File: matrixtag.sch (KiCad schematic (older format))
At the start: 23 parts

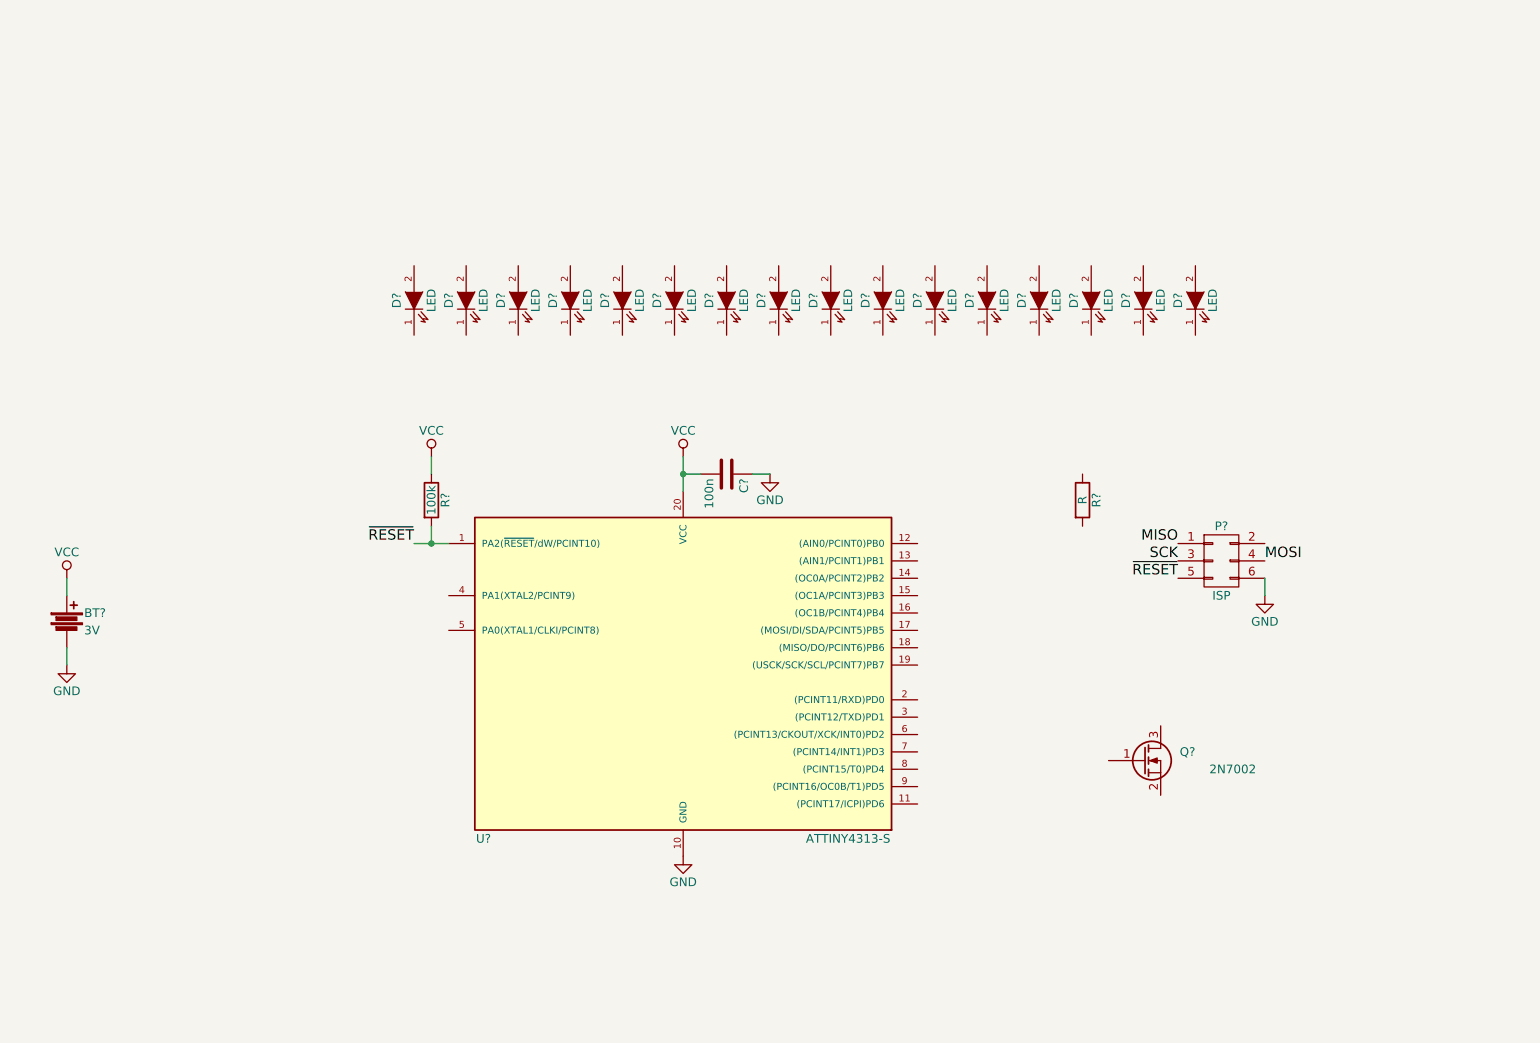
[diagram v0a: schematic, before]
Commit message: Added schematics and unrouted PCB of matrix display nametag
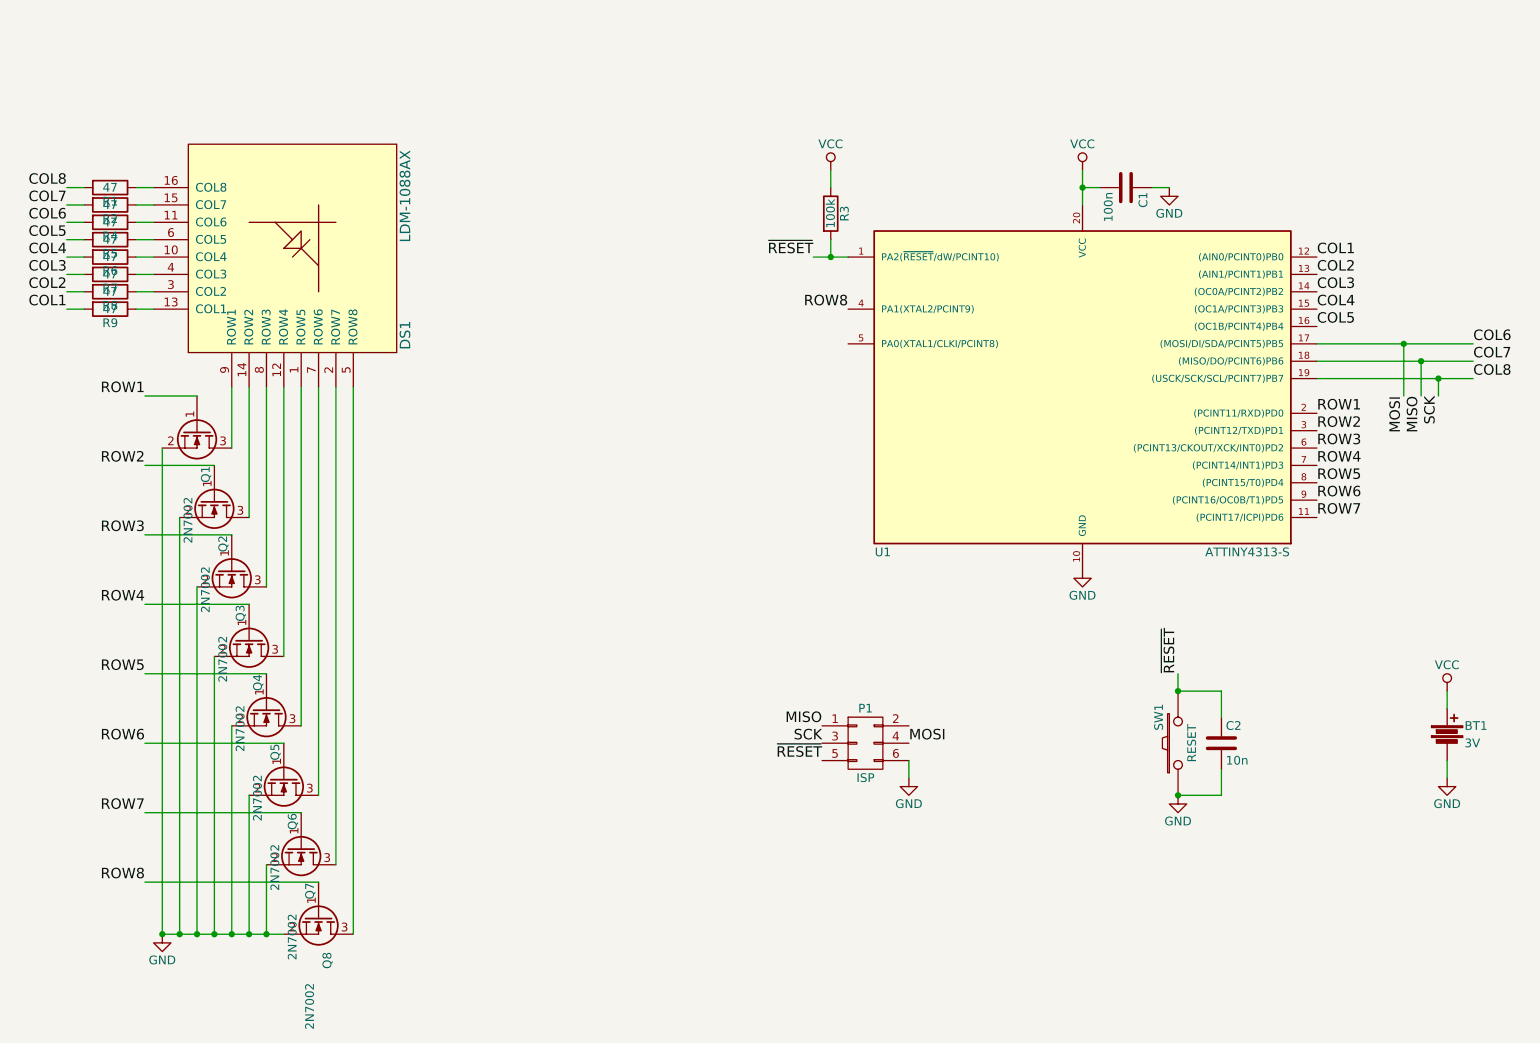
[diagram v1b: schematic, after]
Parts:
- removed D? (x16): LED, symbol LED
- added C2: 10n, Capacitors_SMD:C_0805_HandSoldering, symbol C
- added DS1: LDM-1088AX, nametag:LDM-1088, symbol LDM-1088AX
- added Q2, Q3, Q4, Q5, Q6, Q7, Q8: 2N7002, TO_SOT_Packages_SMD:SOT-23_Handsoldering, symbol Q_NMOS_GSD
- added R2, R4, R5, R6, R7, R8, R9: 47, Resistors_SMD:R_0805_HandSoldering, symbol R
- added SW1: RESET, Buttons_Switches_ThroughHole:SW_PUSH_SMALL, symbol SW_PUSH
- BT1: renamed from BT?; footprint (none) -> nametag:CR2032
- C1: renamed from C?; footprint (none) -> Capacitors_SMD:C_0805_HandSoldering
- P1: renamed from P?; footprint (none) -> Pin_Headers:Pin_Header_Straight_2x03
- Q1: renamed from Q?; footprint (none) -> TO_SOT_Packages_SMD:SOT-23_Handsoldering
- R1: renamed from R?; value R -> 47; footprint (none) -> Resistors_SMD:R_0805_HandSoldering
- R3: renamed from R?; footprint (none) -> Resistors_SMD:R_0805_HandSoldering
- U1: renamed from U?; footprint SO20 -> Housings_SOIC:SOIC-20_7.5x12.8mm_Pitch1.27mm
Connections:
- net MISO is gone; now on net COL7: P1.1 (P1)
- net MOSI is gone; now on net COL6: P1.4 (P4)
- net SCK is gone; now on net COL8: P1.3 (P3)
- net GND: now also Q1.2 (S), C2.2, Q2.2 (S), Q3.2 (S), Q4.2 (S), Q5.2 (S), Q6.2 (S), Q7.2 (S), Q8.2 (S), SW1.1
- net ~RESET: now also C2.1, SW1.2
- net ROW1: now reaches Q1.1 (G)
- net ROW1: now also U1.2 ((PCINT11/RXD)PD0)
- net at Q1.3 (D): now also DS1.9 (ROW1)
- net ROW7: now reaches U1.11 ((PCINT17/ICPI)PD6)
- net ROW7: now also Q7.1 (G)
- net COL1: now reaches U1.12 ((AIN0/PCINT0)PB0)
- net COL1: now also R9.2
- net COL2: now reaches U1.13 ((AIN1/PCINT1)PB1)
- net COL2: now also R8.2
- net COL3: now reaches U1.14 ((OC0A/PCINT2)PB2)
- net COL3: now also R7.2
- net COL4: now reaches U1.15 ((OC1A/PCINT3)PB3)
- net COL4: now also R6.2
- net COL5: now reaches U1.16 ((OC1B/PCINT4)PB4)
- net COL5: now also R5.2
- net COL6: now reaches U1.17 ((MOSI/DI/SDA/PCINT5)PB5)
- net COL6: now also R4.2
- net COL7: now reaches U1.18 ((MISO/DO/PCINT6)PB6)
- net COL7: now also R2.2
- net COL8: now reaches U1.19 ((USCK/SCK/SCL/PCINT7)PB7)
- net COL8: now also R1.2
- net ROW2: now reaches U1.3 ((PCINT12/TXD)PD1)
- net ROW2: now also Q2.1 (G)
- net ROW8: now reaches U1.4 (PA1(XTAL2/PCINT9))
- net ROW8: now also Q8.1 (G)
- net ROW3: now reaches U1.6 ((PCINT13/CKOUT/XCK/INT0)PD2)
- net ROW3: now also Q3.1 (G)
- net ROW4: now reaches U1.7 ((PCINT14/INT1)PD3)
- net ROW4: now also Q4.1 (G)
- net ROW5: now reaches U1.8 ((PCINT15/T0)PD4)
- net ROW5: now also Q5.1 (G)
- net ROW6: now reaches U1.9 ((PCINT16/OC0B/T1)PD5)
- net ROW6: now also Q6.1 (G)
- net at R1.1: now also DS1.16 (COL8)
- new net: DS1.1 (ROW5), Q5.3 (D)
- new net: DS1.10 (COL4), R6.1
- new net: DS1.11 (COL6), R4.1
- new net: DS1.12 (ROW4), Q4.3 (D)
- new net: DS1.13 (COL1), R9.1
- new net: DS1.14 (ROW2), Q2.3 (D)
- new net: DS1.15 (COL7), R2.1
- new net: DS1.2 (ROW7), Q7.3 (D)
- new net: DS1.3 (COL2), R8.1
- new net: DS1.4 (COL3), R7.1
- new net: DS1.5 (ROW8), Q8.3 (D)
- new net: DS1.6 (COL5), R5.1
- new net: DS1.7 (ROW6), Q6.3 (D)
- new net: DS1.8 (ROW3), Q3.3 (D)
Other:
- moved on the sheet: BT1, C1, P1, Q1, R1, R3, U1

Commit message: Finished matrix tag schematic and layout
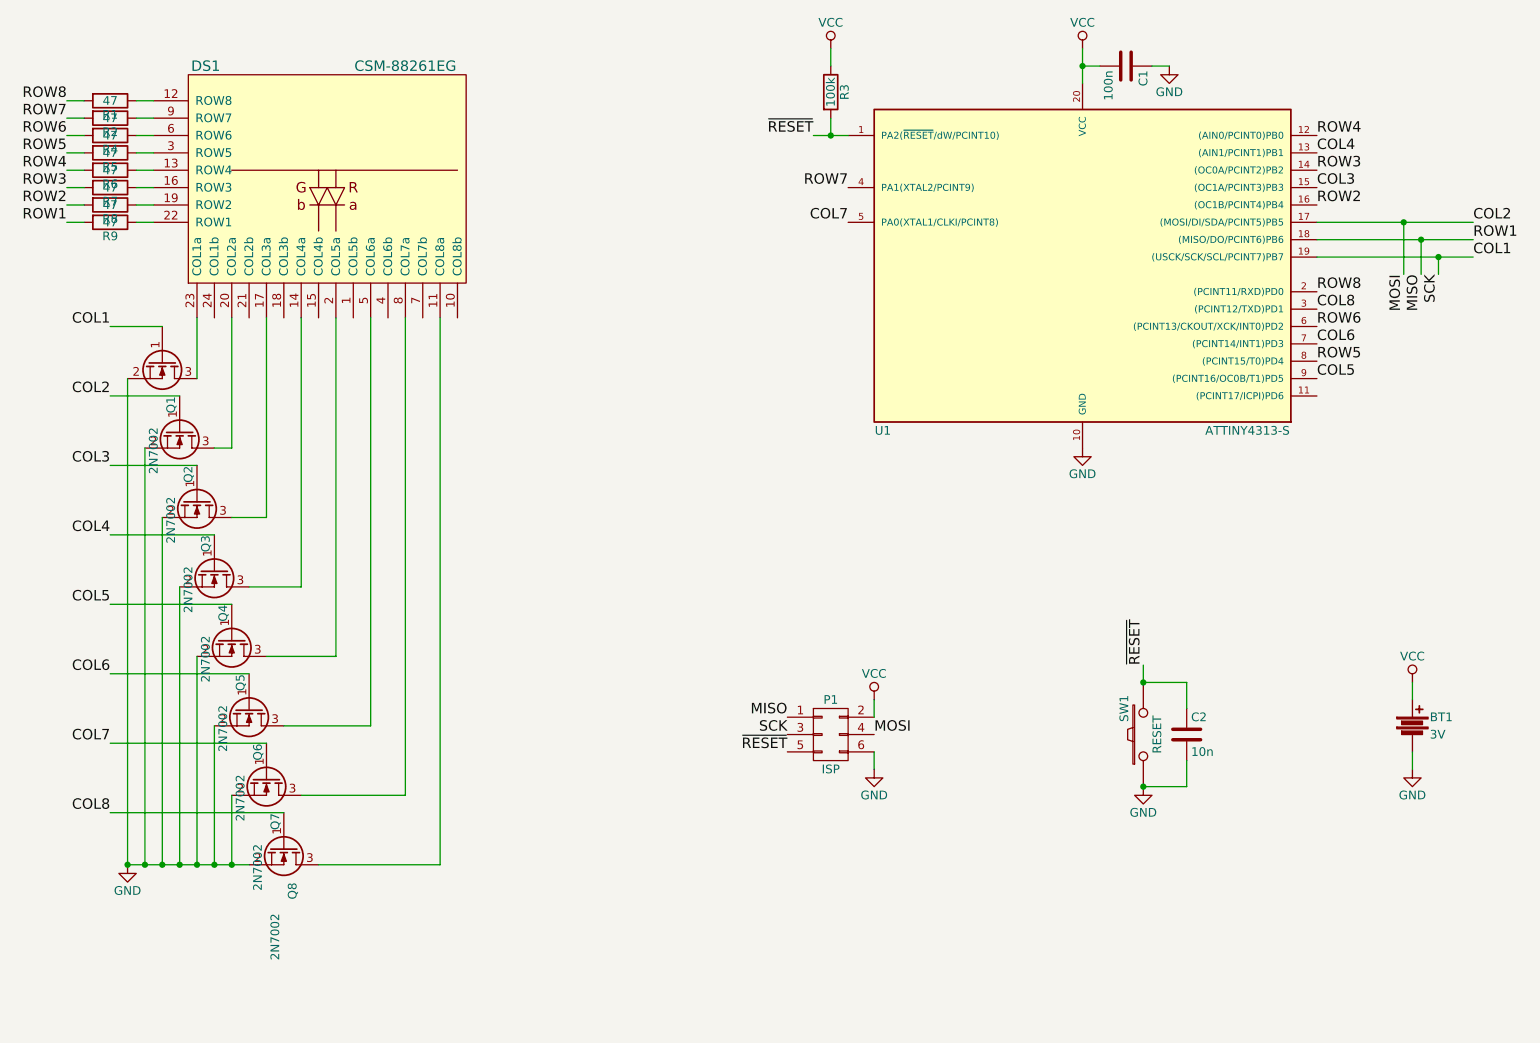
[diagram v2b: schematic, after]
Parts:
- removed DS1: LDM-1088AX, nametag:LDM-1088, symbol LDM-1088AX
- added DS1: CSM-88261EG, nametag:CSM-88261, symbol CSM-88261EG
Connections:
- net COL1: now also P1.3 (P3), Q1.1 (G), U1.19 ((USCK/SCK/SCL/PCINT7)PB7); no longer R9.2, U1.12 ((AIN0/PCINT0)PB0)
- net COL2: now also P1.4 (P4), Q2.1 (G), U1.17 ((MOSI/DI/SDA/PCINT5)PB5); no longer R8.2, U1.13 ((AIN1/PCINT1)PB1)
- net COL3: now also Q3.1 (G), U1.15 ((OC1A/PCINT3)PB3); no longer R7.2, U1.14 ((OC0A/PCINT2)PB2)
- net COL4: now also Q4.1 (G), U1.13 ((AIN1/PCINT1)PB1); no longer R6.2, U1.15 ((OC1A/PCINT3)PB3)
- net COL5: now also Q5.1 (G), U1.9 ((PCINT16/OC0B/T1)PD5); no longer R5.2, U1.16 ((OC1B/PCINT4)PB4)
- net COL6: now also Q6.1 (G), U1.7 ((PCINT14/INT1)PD3); no longer P1.4 (P4), R4.2, U1.17 ((MOSI/DI/SDA/PCINT5)PB5)
- net COL7: now also Q7.1 (G), U1.5 (PA0(XTAL1/CLKI/PCINT8)); no longer P1.1 (P1), R2.2, U1.18 ((MISO/DO/PCINT6)PB6)
- net COL8: now also Q8.1 (G), U1.3 ((PCINT12/TXD)PD1); no longer P1.3 (P3), R1.2, U1.19 ((USCK/SCK/SCL/PCINT7)PB7)
- net ROW2: now also R8.2, U1.16 ((OC1B/PCINT4)PB4); no longer Q2.1 (G), U1.3 ((PCINT12/TXD)PD1)
- net ROW3: now also R7.2, U1.14 ((OC0A/PCINT2)PB2); no longer Q3.1 (G), U1.6 ((PCINT13/CKOUT/XCK/INT0)PD2)
- net ROW4: now also R6.2, U1.12 ((AIN0/PCINT0)PB0); no longer Q4.1 (G), U1.7 ((PCINT14/INT1)PD3)
- net ROW5: now also R5.2; no longer Q5.1 (G)
- net ROW6: now also R4.2, U1.6 ((PCINT13/CKOUT/XCK/INT0)PD2); no longer Q6.1 (G), U1.9 ((PCINT16/OC0B/T1)PD5)
- net ROW7: now also R2.2, U1.4 (PA1(XTAL2/PCINT9)); no longer Q7.1 (G), U1.11 ((PCINT17/ICPI)PD6)
- net ROW8: now also R1.2, U1.2 ((PCINT11/RXD)PD0); no longer Q8.1 (G), U1.4 (PA1(XTAL2/PCINT9))
- net VCC: now also P1.2 (P2)
- net at Q1.3 (D): now also DS1.23 (COL1a)
- net at R1.1: now also DS1.12 (ROW8)
- net at Q5.3 (D): now also DS1.2 (COL5a)
- net at R6.1: now also DS1.13 (ROW4)
- net at R4.1: now also DS1.6 (ROW6)
- net at Q4.3 (D): now also DS1.14 (COL4a)
- net at R9.1: now also DS1.22 (ROW1)
- net at Q2.3 (D): now also DS1.20 (COL2a)
- net at R2.1: now also DS1.9 (ROW7)
- net at Q7.3 (D): now also DS1.8 (COL7a)
- net at R8.1: now also DS1.19 (ROW2)
- net at R7.1: now also DS1.16 (ROW3)
- net at Q8.3 (D): now also DS1.11 (COL8a)
- net at R5.1: now also DS1.3 (ROW5)
- net at Q6.3 (D): now also DS1.5 (COL6a)
- net at Q3.3 (D): now also DS1.17 (COL3a)
- removed net ROW1: Q1.1 (G), U1.2 ((PCINT11/RXD)PD0)
- new net MISO: P1.1 (P1), R9.2, U1.18 ((MISO/DO/PCINT6)PB6)
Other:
- moved on the sheet: BT1, C1, C2, P1, Q1, Q2, Q3, Q4, Q5, Q6, Q7, Q8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

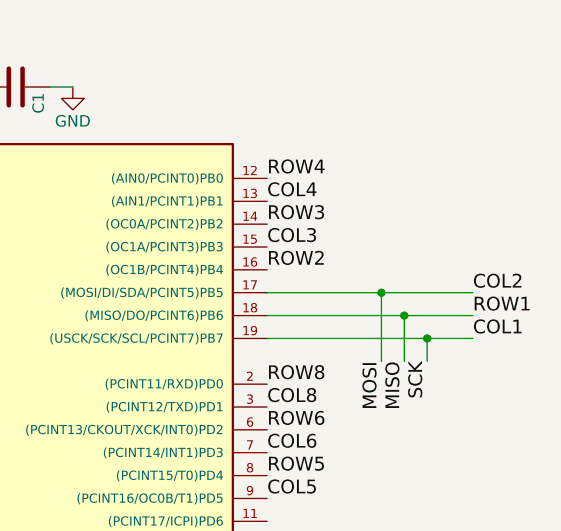
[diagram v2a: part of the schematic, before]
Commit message: Fixed matrix tag layout with correct panel pinout
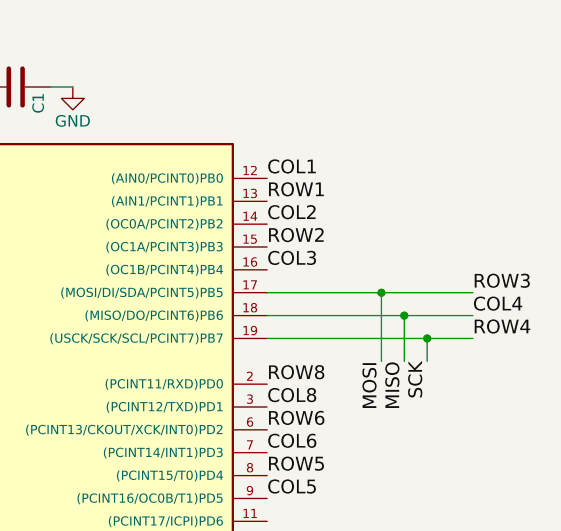
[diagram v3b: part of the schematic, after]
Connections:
- net COL1: now also U1.12 ((AIN0/PCINT0)PB0); no longer P1.3 (P3), U1.19 ((USCK/SCK/SCL/PCINT7)PB7)
- net COL2: now also U1.14 ((OC0A/PCINT2)PB2); no longer P1.4 (P4), U1.17 ((MOSI/DI/SDA/PCINT5)PB5)
- net COL3: now also U1.16 ((OC1B/PCINT4)PB4); no longer U1.15 ((OC1A/PCINT3)PB3)
- net COL4: now also P1.1 (P1), U1.18 ((MISO/DO/PCINT6)PB6); no longer U1.13 ((AIN1/PCINT1)PB1)
- net ROW2: now also U1.15 ((OC1A/PCINT3)PB3); no longer U1.16 ((OC1B/PCINT4)PB4)
- net ROW4: now also P1.3 (P3), U1.19 ((USCK/SCK/SCL/PCINT7)PB7); no longer U1.12 ((AIN0/PCINT0)PB0)
- removed net MISO: P1.1 (P1), R9.2, U1.18 ((MISO/DO/PCINT6)PB6)
- net ROW3 renamed MOSI
- net MOSI: now also P1.4 (P4), U1.17 ((MOSI/DI/SDA/PCINT5)PB5); no longer U1.14 ((OC0A/PCINT2)PB2)
- new net ROW1: R9.2, U1.13 ((AIN1/PCINT1)PB1)
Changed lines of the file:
@@
 Sheet 1 1
 Title "LED Name Tag"
-Date "2016-04-06"
-Rev "1"
+Date "2016-06-23"
+Rev "2"
 Comp "Chaostreff Basel"
 Comment1 "KiCad Workshop CoSin 2016"
@@
 Wire Wire Line
 	2450 2550 2150 2550
-Text Label 10000 2150 0    60   ~ 0
+Text Label 9100 1450 0    60   ~ 0
 COL1
-Text Label 10000 1950 0    60   ~ 0
+Text Label 9100 1650 0    60   ~ 0
 COL2
-Text Label 9100 1750 0    60   ~ 0
+Text Label 9100 1850 0    60   ~ 0
 COL3
-Text Label 9100 1550 0    60   ~ 0
+Text Label 10000 2050 0    60   ~ 0
 COL4
 Text Label 9100 2850 0    60   ~ 0
@@
 Text Label 9100 2450 0    60   ~ 0
 COL8
-Text Label 10000 2050 0    60   ~ 0
+Text Label 9100 1550 0    60   ~ 0
 ROW1
-Text Label 9100 1850 0    60   ~ 0
+Text Label 9100 1750 0    60   ~ 0
 ROW2
-Text Label 9100 1650 0    60   ~ 0
+Text Label 10000 1950 0    60   ~ 0
 ROW3
-Text Label 9100 1450 0    60   ~ 0
+Text Label 10000 2150 0    60   ~ 0
 ROW4
 Text Label 9100 2750 0    60   ~ 0
